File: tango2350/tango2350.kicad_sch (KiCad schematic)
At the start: 10 parts, among them P1 USB_C_Plug_USB2.0, U1 RP2350_80QFN, U2 NCP1117-3.3_SOT223

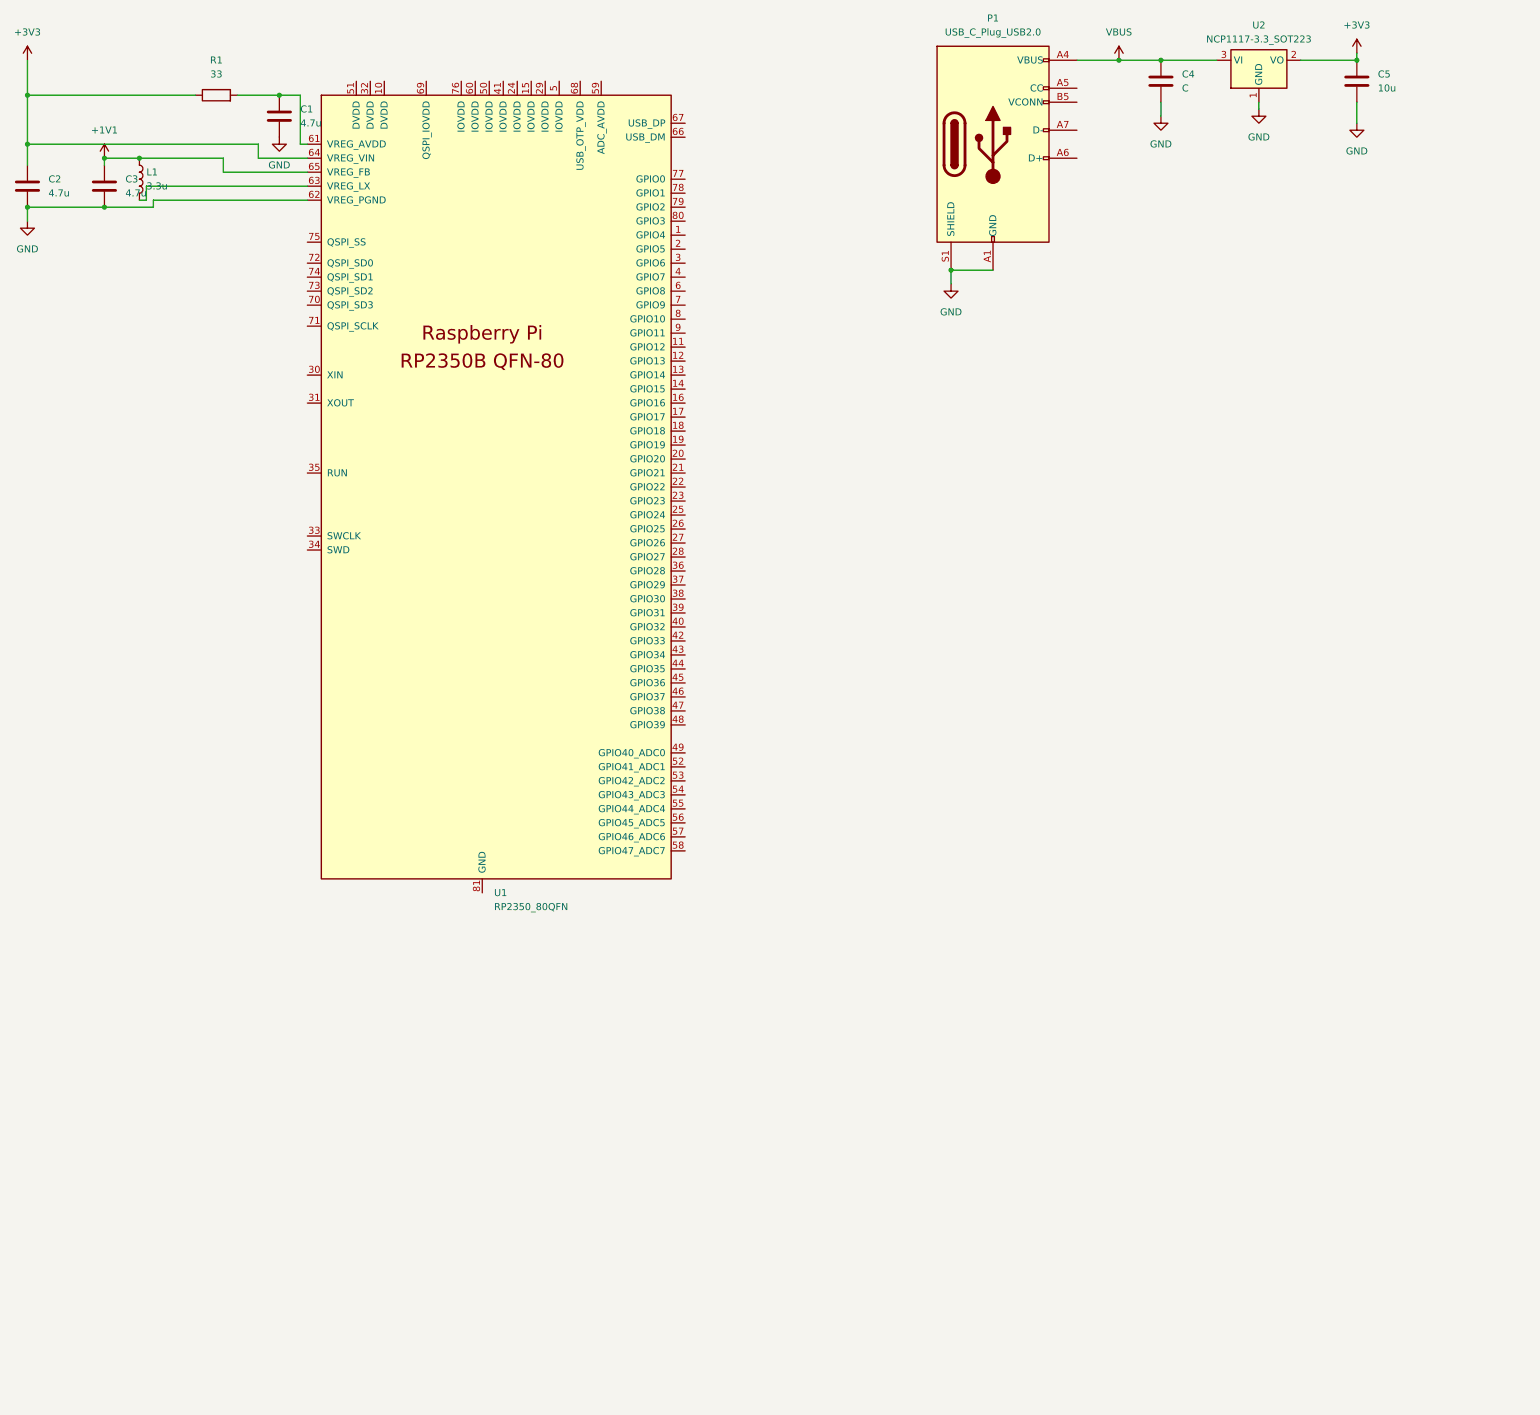
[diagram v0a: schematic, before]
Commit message: Added primary flash, Crystal Oscillator, and GPIO.
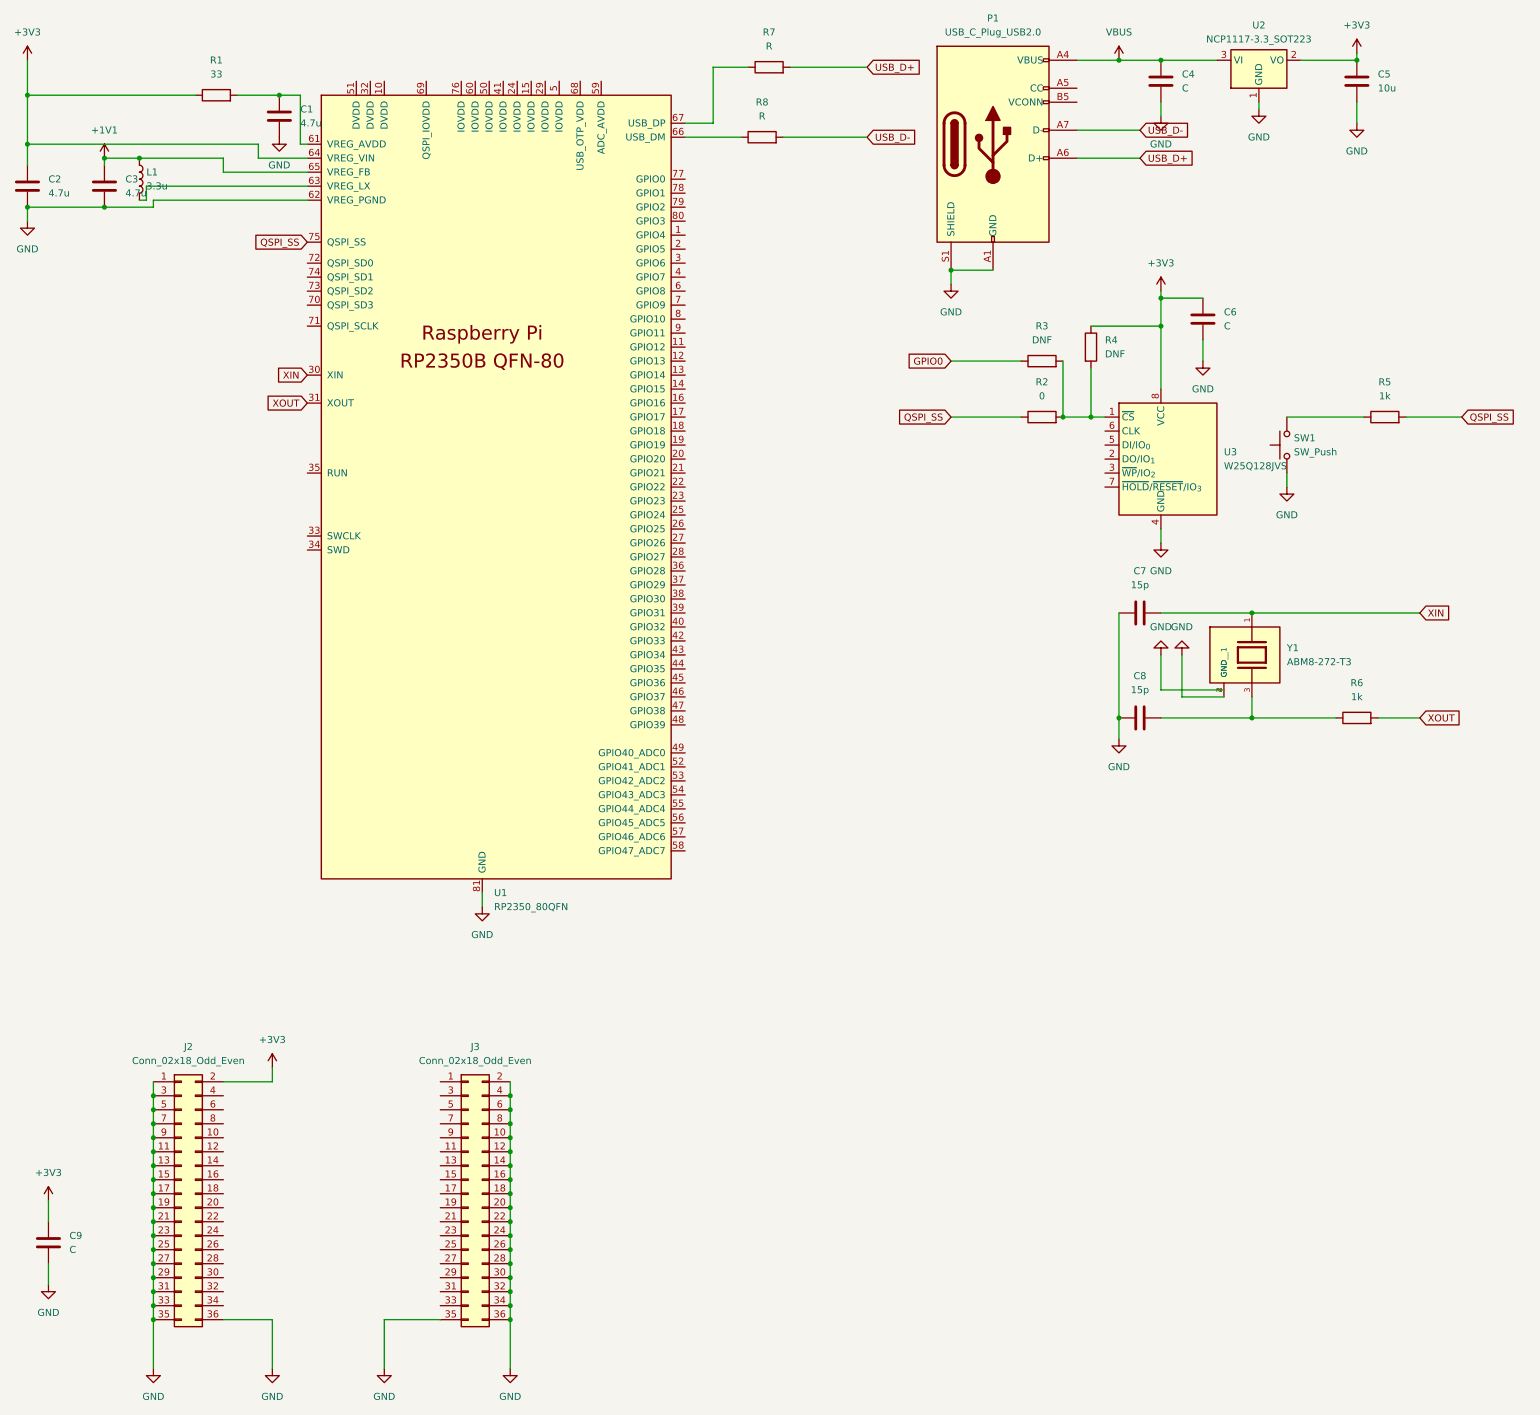
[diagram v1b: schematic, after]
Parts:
- added C6, C9: C, symbol Device:C
- added C7, C8: 15p, symbol Device:C
- added J2, J3: Conn_02x18_Odd_Even, symbol Connector_Generic:Conn_02x18_Odd_Even
- added R2: 0, symbol Device:R
- added R3, R4: DNF, symbol Device:R
- added R5, R6: 1k, symbol Device:R
- added R7, R8: R, symbol Device:R
- added SW1: SW_Push, symbol Switch:SW_Push
- added U3: W25Q128JVS, Package_SO:SOIC-8_5.3x5.3mm_P1.27mm, symbol Memory_Flash:W25Q128JVS
- added Y1: ABM8-272-T3, ABM8-272-T3:XTAL_ABM8-272-T3, symbol ABM8-272-T3:ABM8-272-T3
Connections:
- net +3V3: now also C6.1, C9.1, J2.2 (Pin_2), R4.1, U3.8 (VCC)
- net GND: now also U1.81 (GND), C6.2, C7.2, C8.1, C9.2, J2.1 (Pin_1), J2.11 (Pin_11), J2.13 (Pin_13), J2.15 (Pin_15), J2.17 (Pin_17), J2.19 (Pin_19), J2.21 (Pin_21), J2.23 (Pin_23), J2.25 (Pin_25), J2.27 (Pin_27), J2.29 (Pin_29), J2.3 (Pin_3), J2.31 (Pin_31), J2.33 (Pin_33), J2.35 (Pin_35), J2.36 (Pin_36), J2.5 (Pin_5), J2.7 (Pin_7), J2.9 (Pin_9), J3.10 (Pin_10), J3.12 (Pin_12), J3.14 (Pin_14), J3.16 (Pin_16), J3.18 (Pin_18), J3.2 (Pin_2), J3.20 (Pin_20), J3.22 (Pin_22), J3.24 (Pin_24), J3.26 (Pin_26), J3.28 (Pin_28), J3.30 (Pin_30), J3.32 (Pin_32), J3.34 (Pin_34), J3.35 (Pin_35), J3.36 (Pin_36), J3.4 (Pin_4), J3.6 (Pin_6), J3.8 (Pin_8), SW1.1, U3.4 (GND), Y1.2 (GND), Y1.4 (GND__1)
- net USB_D+: now reaches P1.A6 (D+)
- net USB_D+: now also R7.2
- net USB_D-: now reaches P1.A7 (D-)
- net USB_D-: now also R8.2
- net XIN: now reaches U1.30 (XIN)
- net XIN: now also C7.1, Y1.1
- net XOUT: now reaches U1.31 (XOUT)
- net XOUT: now also R6.2
- net at U1.66 (USB_DM): now also R8.1
- net at U1.67 (USB_DP): now also R7.1
- net QSPI_SS: now reaches U1.75 (QSPI_SS)
- net QSPI_SS: now also R2.1, R5.2
- new net: R2.2, R3.2, R4.2, U3.1 (~{CS})
- new net: R5.1, SW1.2
- new net: C8.2, R6.1, Y1.3
- new net GPIO0: R3.1

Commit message: Fixed some bugs pointed out by electronic rules checker. Some persistent bugs still remain mostly in the power delivery systems.
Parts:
- removed SW1: SW_Push, symbol Switch:SW_Push
- added C10, C11, C12, C13, C17, C18, C19, C20: 100nF, symbol Device:C
- added C14, C16: 2.2uF, symbol Device:C
- added C15: 10uF, symbol Device:C
- added D1: D, symbol Device:D
- added R10, R9: 5k1, symbol Device:R
- added R11: 1k, symbol Device:R
- added R12, R13, R14: R, symbol Device:R
- added SW2: SW_SPST, symbol Switch:SW_SPST
- C1, C2, C3: value 4.7u -> 100nF
- C4, C9: value C -> 10u
- C6: value C -> 100n
- L1: value 3.3u -> L
- R1: value 33 -> 27R4
- R5: value 1k -> R
- R7, R8: value R -> 27
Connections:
- net +1V1: now also L1.2, U1.10 (DVDD), U1.32 (DVDD), U1.51 (DVDD), C17.1, C18.1, C19.1, C20.1; no longer C3.1, L1.1
- net +3V3: now also C1.2, C2.2, C3.1, R5.2, U1.68 (USB_OTP_VDD), U1.69 (QSPI_IOVDD), U1.76 (IOVDD), C10.2, C11.2, C12.2, C13.2, C15.2, R12.1; no longer C2.1
- net GND: now also C1.1, C2.1, C10.1, C11.1, C12.1, C13.1, C14.1, C15.1, C16.1, C17.2, C18.2, C19.2, C20.2, R10.2, R9.2, SW2.2 (B); no longer C1.2, C2.2
- net GPIO0: now also J2.4 (Pin_4), U1.77 (GPIO0)
- net QSPI_SS: now also D1.2 (A); no longer R5.2
- net at R5.1: now also U1.59 (ADC_AVDD), C16.2
- net VREG_AVDD: now reaches R1.2, U1.61 (VREG_AVDD)
- net VREG_AVDD: now also C14.2; no longer C1.1
- net at U1.63 (VREG_LX): now also L1.1; no longer L1.2
- net at P1.A5 (CC): now also R9.1
- net at P1.B5 (VCONN): now also R10.1
- net GPIO4: now reaches U1.1 (GPIO4)
- net GPIO4: now also J2.12 (Pin_12)
- net GPIO12: now reaches U1.11 (GPIO12)
- net GPIO12: now also J2.28 (Pin_28)
- net GPIO13: now reaches U1.12 (GPIO13)
- net GPIO13: now also J2.30 (Pin_30)
- net GPIO14: now reaches U1.13 (GPIO14)
- net GPIO14: now also J2.32 (Pin_32)
- net GPIO15: now reaches U1.14 (GPIO15)
- net GPIO15: now also J2.34 (Pin_34)
- net GPIO16: now reaches U1.16 (GPIO16)
- net GPIO16: now also J3.27 (Pin_27)
- net GPIO17: now reaches U1.17 (GPIO17)
- net GPIO17: now also J3.25 (Pin_25)
- net GPIO18: now reaches U1.18 (GPIO18)
- net GPIO18: now also J3.23 (Pin_23)
- net GPIO19: now reaches U1.19 (GPIO19)
- net GPIO19: now also J3.21 (Pin_21)
- net GPIO5: now reaches U1.2 (GPIO5)
- net GPIO5: now also J2.14 (Pin_14)
- net GPIO20: now reaches U1.20 (GPIO20)
- net GPIO20: now also J3.19 (Pin_19)
- net GPIO21: now reaches U1.21 (GPIO21)
- net GPIO21: now also J3.17 (Pin_17)
- net GPIO22: now reaches U1.22 (GPIO22)
- net GPIO22: now also J3.15 (Pin_15)
- net GPIO23: now reaches U1.23 (GPIO23)
- net GPIO23: now also J3.13 (Pin_13)
- net GPIO24: now reaches U1.25 (GPIO24)
- net GPIO24: now also J3.11 (Pin_11)
- net GPIO25: now reaches U1.26 (GPIO25)
- net GPIO25: now also J3.9 (Pin_9)
- net USER_SW: now reaches U1.27 (GPIO26)
- net USER_SW: now also R14.1
- net GPIO6: now reaches U1.3 (GPIO6)
- net GPIO6: now also J2.16 (Pin_16)
- net SWCLK: now reaches U1.33 (SWCLK)
- net SWCLK: now also J3.33 (Pin_33)
- net SWD: now reaches U1.34 (SWD)
- net SWD: now also J3.31 (Pin_31)
- net RUN: now reaches U1.35 (RUN)
- net RUN: now also J3.29 (Pin_29)
- net GPIO7: now reaches U1.4 (GPIO7)
- net GPIO7: now also J2.18 (Pin_18)
- net GPIO40_ADC0: now reaches U1.49 (GPIO40_ADC0)
- net GPIO40_ADC0: now also J3.7 (Pin_7)
- net GPIO41_ADC1: now reaches U1.52 (GPIO41_ADC1)
- net GPIO41_ADC1: now also J3.5 (Pin_5)
- net GPIO42_ADC2: now reaches U1.53 (GPIO42_ADC2)
- net GPIO42_ADC2: now also J3.3 (Pin_3)
- net GPIO43_ADC3: now reaches U1.54 (GPIO43_ADC3)
- net GPIO43_ADC3: now also J3.1 (Pin_1)
- net GPIO8: now reaches U1.6 (GPIO8)
- net GPIO8: now also J2.20 (Pin_20)
- net GPIO9: now reaches U1.7 (GPIO9)
- net GPIO9: now also J2.22 (Pin_22)
- net QSPI_SD3: now reaches U1.70 (QSPI_SD3)
- net QSPI_SD3: now also U3.7 (~{HOLD}/~{RESET}/IO_{3})
- net QSPI_SCLK: now reaches U1.71 (QSPI_SCLK)
- net QSPI_SCLK: now also U3.6 (CLK)
- net QSPI_SD0: now reaches U1.72 (QSPI_SD0)
- net QSPI_SD0: now also U3.5 (DI/IO_{0})
- net QSPI_SD2: now reaches U1.73 (QSPI_SD2)
- net QSPI_SD2: now also U3.3 (~{WP}/IO_{2})
- net QSPI_SD1: now reaches U1.74 (QSPI_SD1)
- net QSPI_SD1: now also U3.2 (DO/IO_{1})
- net GPIO1: now reaches U1.78 (GPIO1)
- net GPIO1: now also J2.6 (Pin_6)
- net GPIO2: now reaches U1.79 (GPIO2)
- net GPIO2: now also J2.8 (Pin_8)
- net GPIO10: now reaches U1.8 (GPIO10)
- net GPIO10: now also J2.24 (Pin_24)
- net GPIO3: now reaches U1.80 (GPIO3)
- net GPIO3: now also J2.10 (Pin_10)
- net GPIO11: now reaches U1.9 (GPIO11)
- net GPIO11: now also J2.26 (Pin_26)
- new net: R13.2, R14.2
- new net: R11.2, R12.2, R13.1, SW2.1 (A)
- new net: D1.1 (K), R11.1
- no-connect marks 0 -> 24
